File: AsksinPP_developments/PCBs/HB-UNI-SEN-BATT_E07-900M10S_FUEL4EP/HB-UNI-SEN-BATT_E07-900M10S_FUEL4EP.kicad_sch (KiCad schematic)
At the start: 31 parts, among them J1 Conn_01x02, J10 charge, J11 ePaper connector, J2 Conn_01x02, J3 Conn_01x02, J4 Conn_01x02, J5 ISP Programmer, J6 Conn_01x04, J7 Conn_01x04, J8 Conn_01x04, J9 Conn_01x04, Q1 IRLU024N, SW1 config button

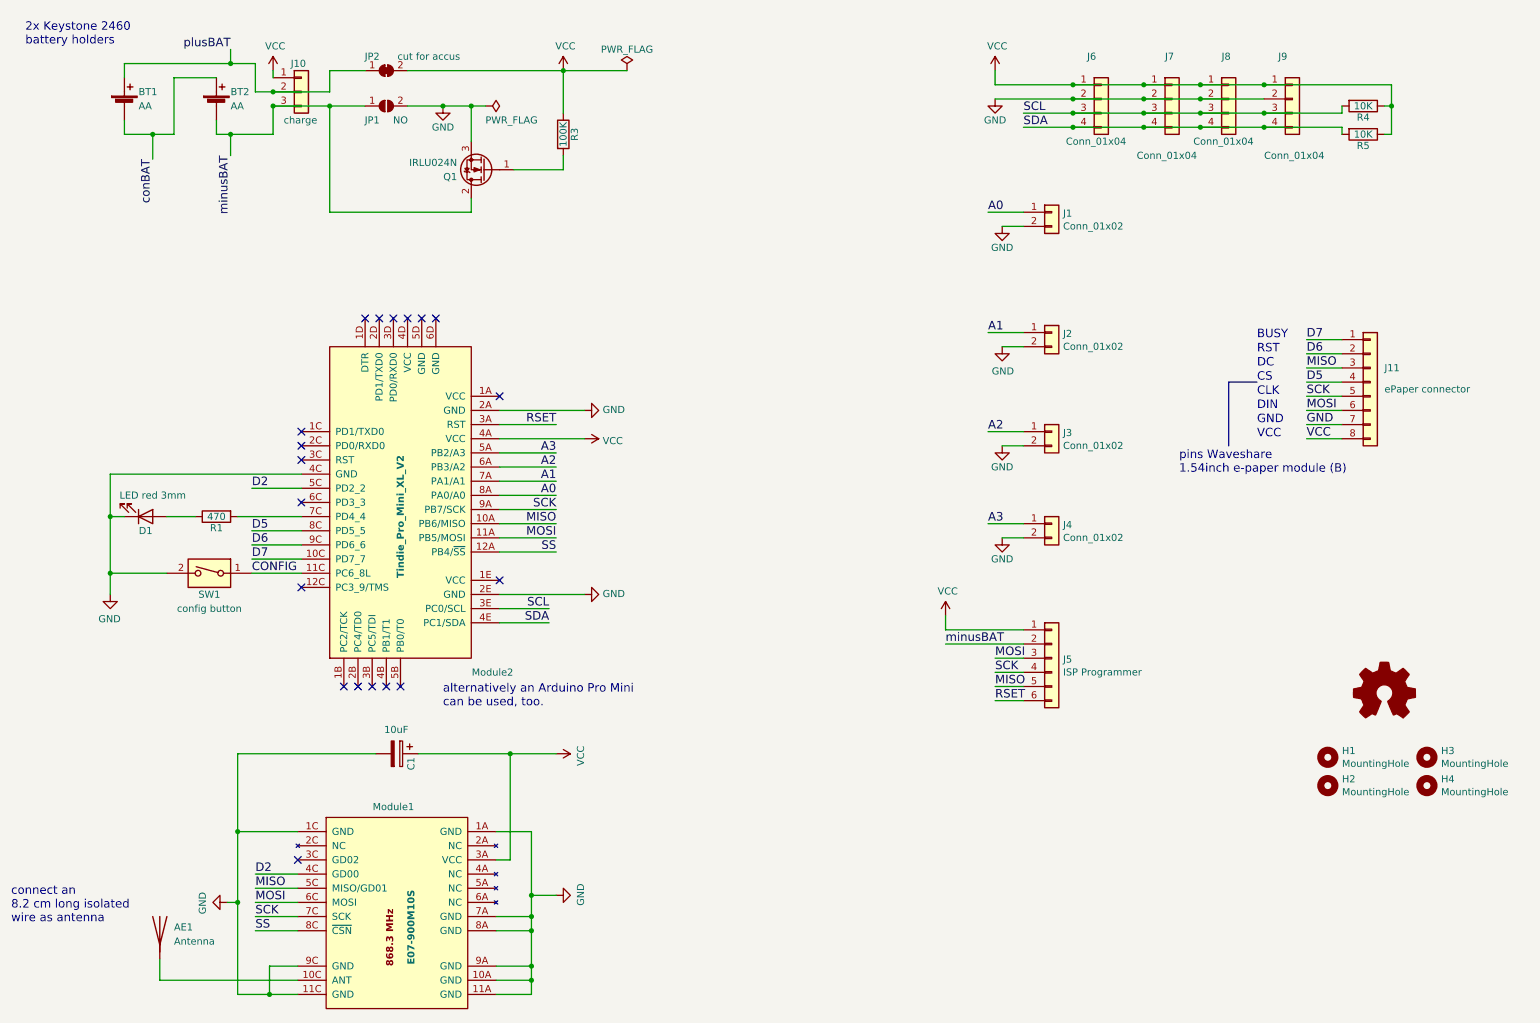
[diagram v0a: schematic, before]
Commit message: PCBs/HB-UNI-SEN-BATT_E07-868MS10_FUEL4EP: migration to KiCAD 8
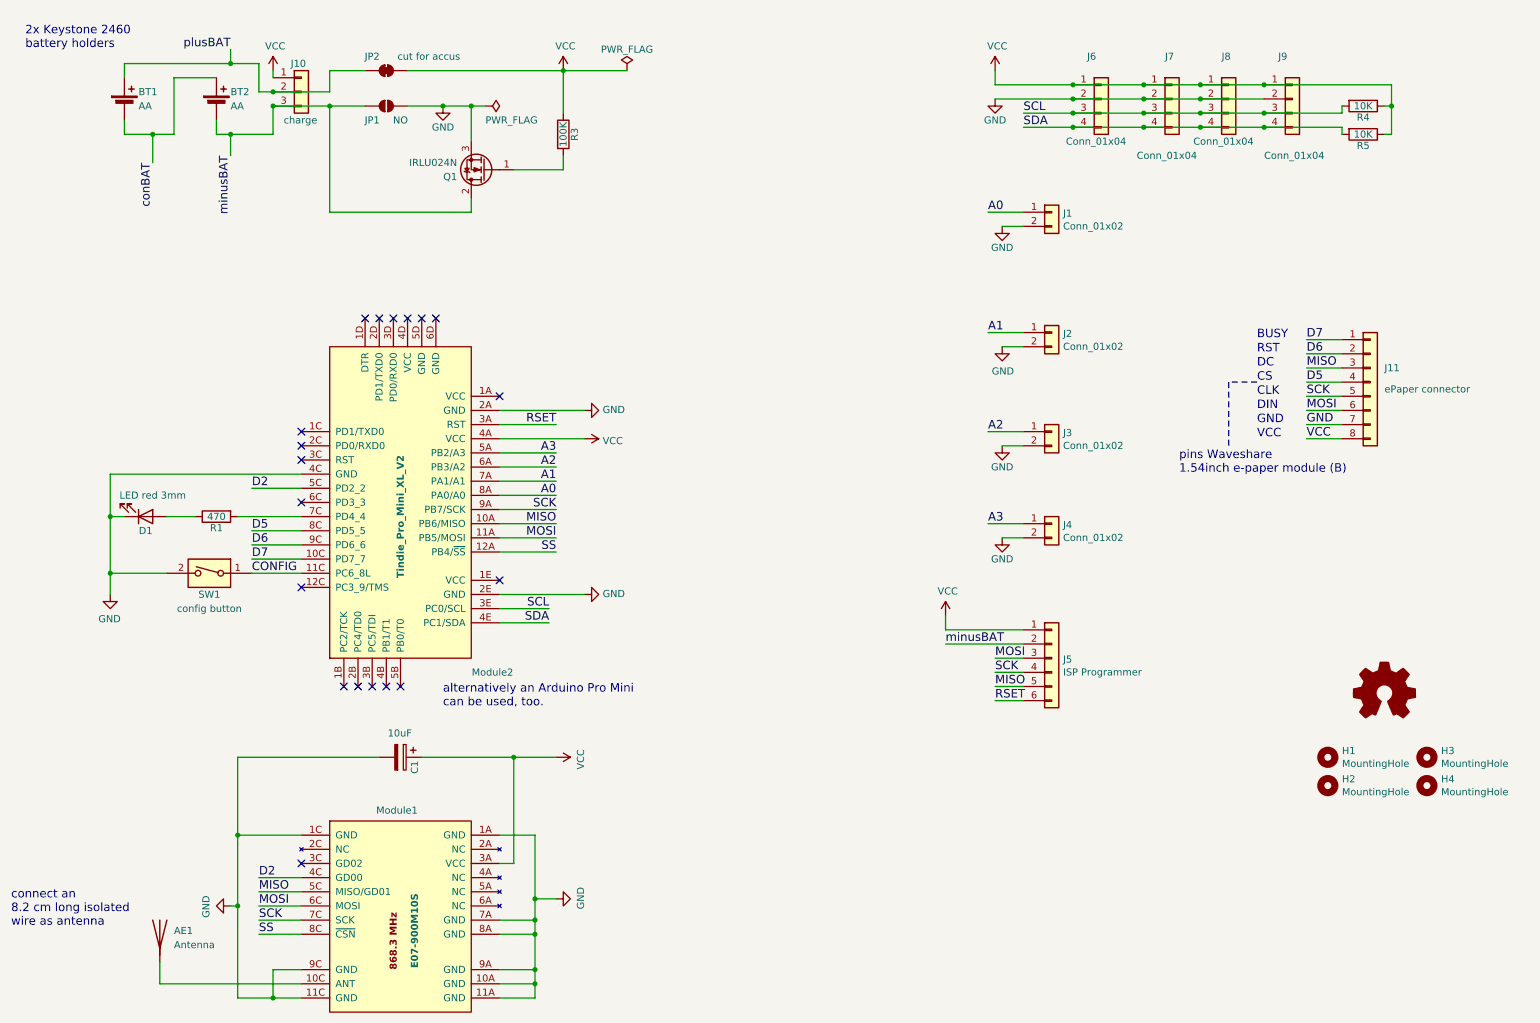
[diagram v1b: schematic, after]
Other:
- moved on the sheet: AE1, C1, Module1

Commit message: update of PCBs/HB-UNI-SEN-BATT_E07-868MS10_FUEL4EP, PCBs/HB-UNI-SEN-BATT_E07-900M10S_FUEL4EP, and PCBs/HB-UNI-SEN-BATT_E07-900MM10S_FUEL4EP to support HB_Pro_Mini_ATMEGA1284P_FUEL4EP
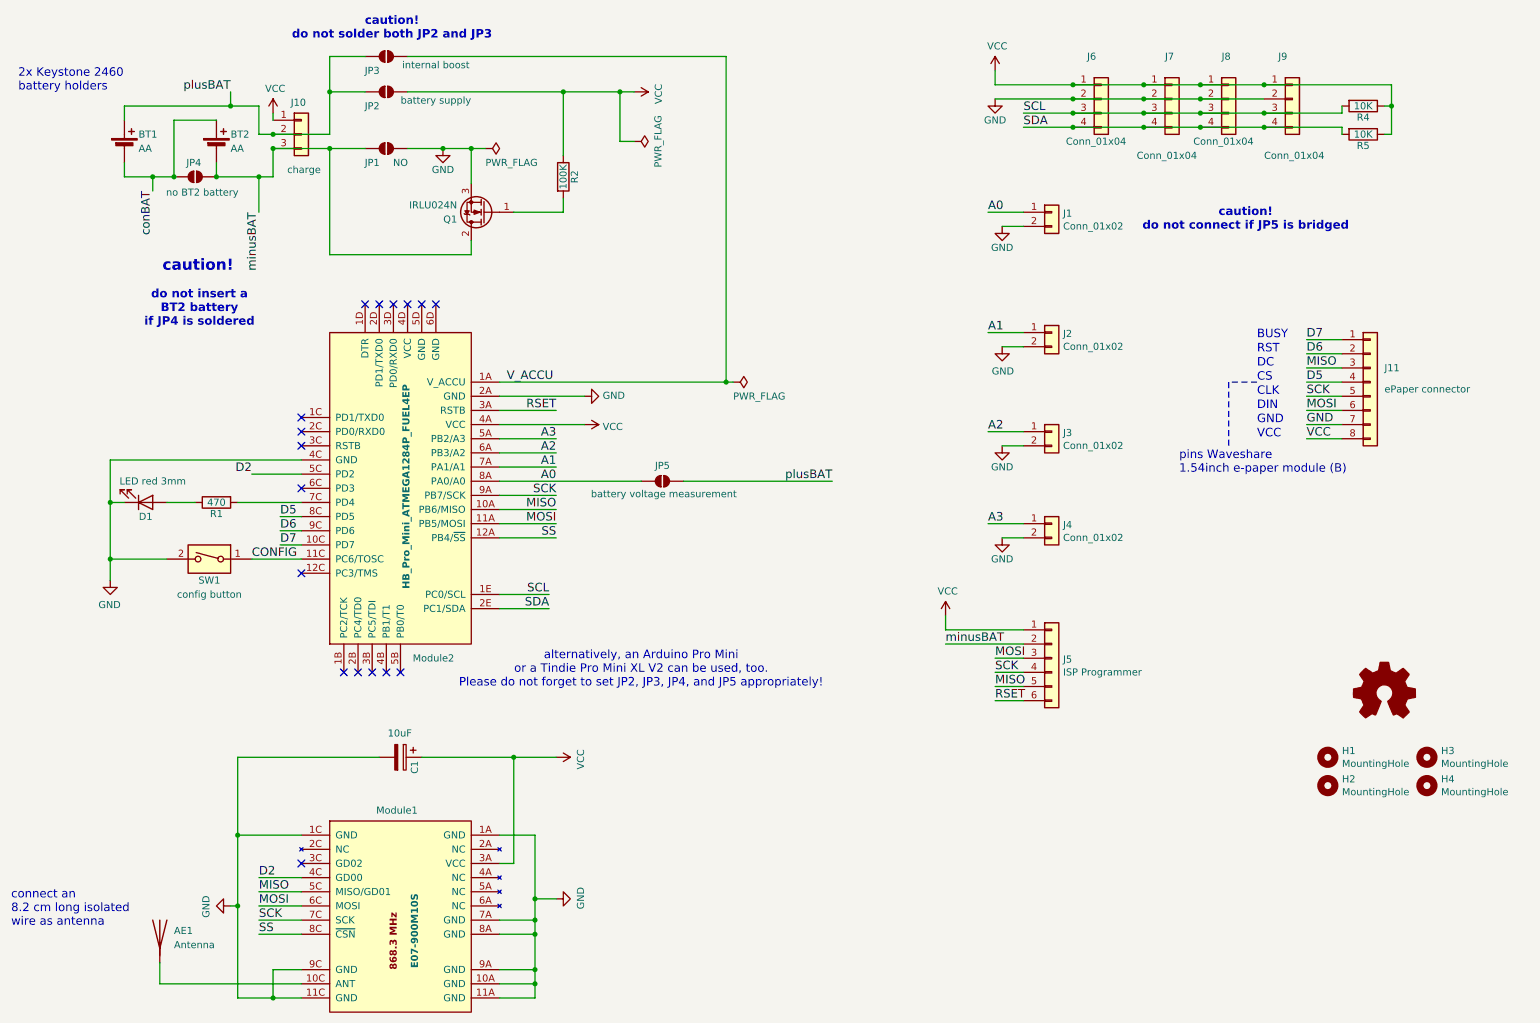
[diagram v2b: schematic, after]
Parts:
- removed JP2: cut for accus, Jumper:SolderJumper-2_P1.3mm_Bridged_Pad1.0x1.5mm, symbol Jumper:SolderJumper_2_Bridged
- removed Module2: Tindie_Pro_Mini_XL_V2, FUEL4EP:Tindie_ArduinoProMiniXL_1284P_V2, symbol FUEL4EP:Tindie_Pro_Mini_XL_V2
- removed R3: 100K, Resistor_THT:R_Axial_DIN0207_L6.3mm_D2.5mm_P2.54mm_Vertical, symbol Device:R
- added JP2: battery supply, Jumper:SolderJumper-2_P1.3mm_Open_Pad1.0x1.5mm, symbol Jumper:SolderJumper_2_Open
- added JP3: internal boost, Jumper:SolderJumper-2_P1.3mm_Open_Pad1.0x1.5mm, symbol Jumper:SolderJumper_2_Open
- added JP4: no BT2 battery, FUEL4EP:SolderJumper-2_P1.3mm_Open_Pad1.0x1.5mm, symbol Jumper:SolderJumper_2_Open
- added JP5: battery voltage measurement, Jumper:SolderJumper-2_P1.3mm_Open_Pad1.0x1.5mm, symbol Jumper:SolderJumper_2_Open
- added Module2: HB_Pro_Mini_ATMEGA1284P_FUEL4EP, FUEL4EP:HB_Pro_Mini_ATMEGA1284P_FUEL4EP, symbol FUEL4EP:HB_Pro_Mini_ATMEGA1284P_FUEL4EP
- added R2: 100K, Resistor_THT:R_Axial_DIN0207_L6.3mm_D2.5mm_P2.54mm_Vertical, symbol Device:R
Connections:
- net A0: now also JP5.1 (A), Module2.8A (PA0/A0)
- net A1: now also Module2.7A (PA1/A1)
- net A2: now also Module2.6A (PB3/A2)
- net A3: now also Module2.5A (PB2/A3)
- net CONFIG: now also Module2.11C (PC6/TOSC)
- net D2: now also Module2.5C (PD2)
- net D5: now also Module2.8C (PD5)
- net D6: now also Module2.9C (PD6)
- net D7: now also Module2.10C (PD7)
- net GND: now also Module2.2A (GND), Module2.4C (GND)
- net MISO: now also Module2.10A (PB6/MISO)
- net MOSI: now also Module2.11A (PB5/MOSI)
- net RSET: now also Module2.3A (RSTB)
- net SCK: now also Module2.9A (PB7/SCK)
- net SCL: now also Module2.1E (PC0/SCL)
- net SDA: now also Module2.2E (PC1/SDA)
- net SS: now also Module2.12A (PB4/~{SS})
- net VCC: now also JP2.2 (B), Module2.4A (VCC), R2.1
- net conBAT: now also JP4.1 (A)
- net minusBAT: now also JP4.2 (B)
- net plusBAT: now also JP2.1 (A), JP3.1 (A), JP5.2 (B)
- net at R1.2: now also Module2.7C (PD4)
- net at Q1.1 (G): now also R2.2
- new net V_ACCU: JP3.2 (B), Module2.1A (V_ACCU)
- no-connect marks 19 -> 17
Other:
- note added: "alternatively, an Arduino Pro Mini or a Tindie Pro Mini XL V2 can be used, too. Please do not forget to set JP2, JP3, JP4, and JP5 appropriately!"
- note added: "caution!"
- note added: "caution! do not connect if JP5 is bridged"
- note added: "caution! do not solder both JP2 and JP3"
- note added: "do not insert a BT2 battery if JP4 is soldered"
- note removed: "alternatively an Arduino Pro Mini can be used, too."
- company: FUEL4EP -> (C) FUEL4EP 2025
